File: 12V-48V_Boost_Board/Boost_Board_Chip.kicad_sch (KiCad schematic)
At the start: 23 parts, among them Q1 FDWS86068-F085

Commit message: Made all the changes, still working on the refining the track sizes
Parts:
- renumbered R8 to R10, R9 to R11, R3 to R5, R4 to R6, R5 to R7, R6 to R8, R7 to R9
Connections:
- net at C8.1, R6.2: now also R8.1; no longer R8.2
- net at U1.4 (GATE): now also Q1.4 (G); no longer Q1.3 (G)
- new net: Q1.8 (S), R8.2, R9.1
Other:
- moved on the sheet: Q1, R8
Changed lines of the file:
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@@
 	)
 	(junction
-		(at 175.26 60.96)
-		(diameter 0)
-		(color 0 0 0 0)
-	)
-	(junction
 		(at 172.72 90.17)
 		(diameter 0)
@@
 	)
 	(junction
+		(at 176.53 60.96)
+		(diameter 0)
+		(color 0 0 0 0)
+	)
+	(junction
 		(at 128.27 71.12)
 		(diameter 0)
@@
 	(wire
 		(pts
-			(xy 144.78 71.12) (xy 167.64 71.12)
+			(xy 144.78 71.12) (xy 168.91 71.12)
 		)
 		(stroke
@@
 	(wire
 		(pts
-			(xy 116.84 60.96) (xy 175.26 60.96)
+			(xy 116.84 60.96) (xy 176.53 60.96)
 		)
 		(stroke
@@
 	(wire
 		(pts
-			(xy 43.18 60.96) (xy 52.07 60.96)
+			(xy 176.53 60.96) (xy 196.85 60.96)
 		)
 		(stroke
@@
 	(wire
 		(pts
-			(xy 166.37 93.98) (xy 166.37 124.46)
+			(xy 43.18 60.96) (xy 52.07 60.96)
 		)
 		(stroke
@@
 	(wire
 		(pts
-			(xy 53.34 93.98) (xy 53.34 95.25)
+			(xy 166.37 93.98) (xy 166.37 124.46)
 		)
 		(stroke
@@
 	(wire
 		(pts
-			(xy 43.18 93.98) (xy 53.34 93.98)
+			(xy 53.34 93.98) (xy 53.34 95.25)
 		)
 		(stroke
@@
 	(wire
 		(pts
-			(xy 91.44 64.77) (xy 91.44 60.96)
+			(xy 43.18 93.98) (xy 53.34 93.98)
 		)
 		(stroke
@@
 	(wire
 		(pts
-			(xy 250.19 109.22) (xy 250.19 118.11)
+			(xy 91.44 64.77) (xy 91.44 60.96)
 		)
 		(stroke
@@
 	(wire
 		(pts
-			(xy 52.07 86.36) (xy 52.07 60.96)
+			(xy 250.19 109.22) (xy 250.19 118.11)
 		)
 		(stroke
@@
 	(wire
 		(pts
-			(xy 175.26 76.2) (xy 189.23 76.2)
+			(xy 52.07 86.36) (xy 52.07 60.96)
 		)
 		(stroke
@@
 	(wire
 		(pts
-			(xy 175.26 60.96) (xy 196.85 60.96)
+			(xy 176.53 76.2) (xy 189.23 76.2)
 		)
 		(stroke
@@
 	(wire
 		(pts
-			(xy 175.26 60.96) (xy 175.26 66.04)
+			(xy 176.53 60.96) (xy 176.53 66.04)
 		)
 		(stroke
@@
 		(dnp no)
 		(fields_autoplaced yes)
-		(property "Reference" "R7"
+		(property "Reference" "R9"
 			(at 191.77 101.5999 0)
 			(effects
@@
 			(project "12V-48V_Boost_Board"
 				(path "/3a220cd2-54b9-463d-ba95-4a8308a2a2d6/5e4f9813-0913-4f01-9ef9-037c6221a469"
-					(reference "R7")
+					(reference "R9")
 					(unit 1)
 				)
@@
 		(dnp no)
 		(fields_autoplaced yes)
-		(property "Reference" "R8"
+		(property "Reference" "R10"
 			(at 223.52 81.2799 0)
 			(effects
@@
 			(project "12V-48V_Boost_Board"
 				(path "/3a220cd2-54b9-463d-ba95-4a8308a2a2d6/5e4f9813-0913-4f01-9ef9-037c6221a469"
-					(reference "R8")
+					(reference "R10")
 					(unit 1)
 				)
@@
 	(symbol
 		(lib_id "Device:Q_NMOS_DSG")
-		(at 172.72 71.12 0)
+		(at 173.99 71.12 0)
 		(unit 1)
 		(exclude_from_sim no)
@@
 		(fields_autoplaced yes)
 		(property "Reference" "Q1"
-			(at 179.07 69.8499 0)
+			(at 180.34 69.8499 0)
 			(effects
 				(font
@@
 		)
 		(property "Value" "FDWS86068-F085"
-			(at 179.07 72.3899 0)
+			(at 180.34 72.3899 0)
 			(effects
 				(font
@@
 		)
 		(property "Footprint" "12/48 boost:Q1 Mosfet"
-			(at 177.8 68.58 0)
+			(at 179.07 68.58 0)
 			(effects
 				(font
@@
 		)
 		(property "Datasheet" "https://www.onsemi.com/download/data-sheet/pdf/fdws86068-f085-d.pdf"
-			(at 172.72 71.12 0)
+			(at 173.99 71.12 0)
 			(effects
 				(font
@@
 		)
 		(property "Description" "N-MOSFET transistor, drain/source/gate"
-			(at 172.72 71.12 0)
+			(at 173.99 71.12 0)
 			(effects
 				(font
@@
 		(pin "1"
 		)
-		(pin "2"
+		(pin "4"
 		)
-		(pin "3"
+		(pin "8"
 		)
 		(instances
@@
 		(dnp no)
 		(fields_autoplaced yes)
-		(property "Reference" "R9"
+		(property "Reference" "R11"
 			(at 223.52 129.5399 0)
 			(effects
@@
 			(project "12V-48V_Boost_Board"
 				(path "/3a220cd2-54b9-463d-ba95-4a8308a2a2d6/5e4f9813-0913-4f01-9ef9-037c6221a469"
-					(reference "R9")
+					(reference "R11")
 					(unit 1)
 				)
@@
 		(dnp no)
 		(fields_autoplaced yes)
-		(property "Reference" "R4"
+		(property "Reference" "R6"
 			(at 152.4 83.82 90)
 			(effects
@@
 			(project "12V-48V_Boost_Board"
 				(path "/3a220cd2-54b9-463d-ba95-4a8308a2a2d6/5e4f9813-0913-4f01-9ef9-037c6221a469"
-					(reference "R4")
+					(reference "R6")
 					(unit 1)
 				)
@@
 		(dnp no)
 		(fields_autoplaced yes)
-		(property "Reference" "R3"
+		(property "Reference" "R5"
 			(at 71.12 110.4899 0)
 			(effects
@@
 			(project "12V-48V_Boost_Board"
 				(path "/3a220cd2-54b9-463d-ba95-4a8308a2a2d6/5e4f9813-0913-4f01-9ef9-037c6221a469"
-					(reference "R3")
+					(reference "R5")
 					(unit 1)
 				)
@@
 		(dnp no)
 		(fields_autoplaced yes)
-		(property "Reference" "R5"
+		(property "Reference" "R7"
 			(at 154.94 130.8099 0)
 			(effects
@@
 			(project "12V-48V_Boost_Board"
 				(path "/3a220cd2-54b9-463d-ba95-4a8308a2a2d6/5e4f9813-0913-4f01-9ef9-037c6221a469"
-					(reference "R5")
+					(reference "R7")
 					(unit 1)
 				)
@@
 	(symbol
 		(lib_id "Device:R_US")
-		(at 180.34 90.17 270)
+		(at 180.34 90.17 90)
 		(unit 1)
 		(exclude_from_sim no)
@@
 		(dnp no)
 		(fields_autoplaced yes)
-		(property "Reference" "R6"
+		(property "Reference" "R8"
 			(at 180.34 83.82 90)
 			(effects
@@
 		)
 		(property "Footprint" "Resistor_SMD:R_0805_2012Metric_Pad1.20x1.40mm_HandSolder"
-			(at 180.086 91.186 90)
+			(at 180.594 89.154 90)
 			(effects
 				(font
@@
 			(project "12V-48V_Boost_Board"
 				(path "/3a220cd2-54b9-463d-ba95-4a8308a2a2d6/5e4f9813-0913-4f01-9ef9-037c6221a469"
-					(reference "R6")
+					(reference "R8")
 					(unit 1)
 				)

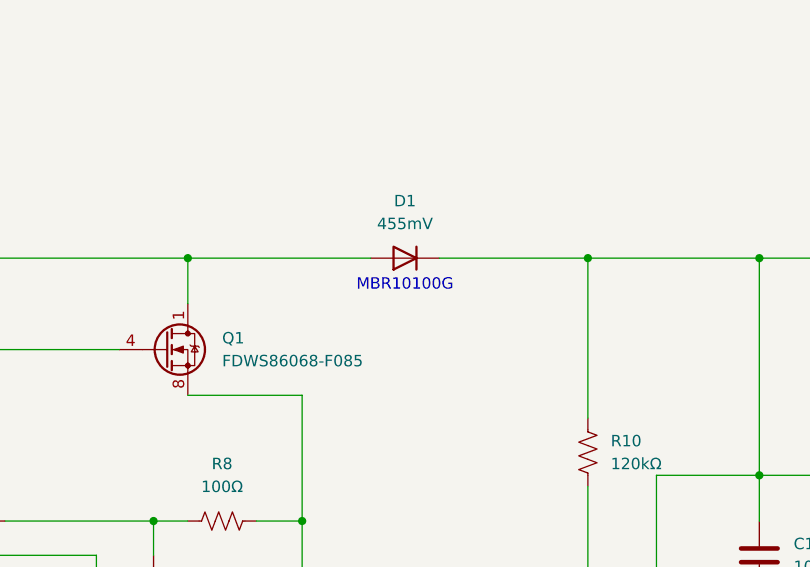
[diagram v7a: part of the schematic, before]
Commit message: Made some changes to track sizes
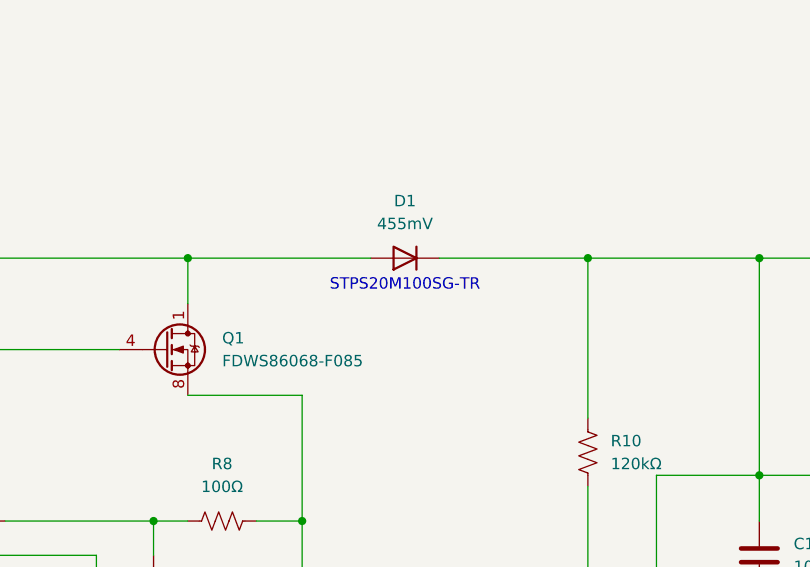
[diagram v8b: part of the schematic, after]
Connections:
- net 48V_OUTPUT: now also D1.3 (K); no longer D1.1 (K)
- net at L1.2, Q1.1 (D): now also D1.1 (A); no longer D1.2 (A)
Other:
- note added: "STPS20M100SG-TR"
- note removed: "MBR10100G"
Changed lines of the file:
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@@
 		)
 	)
-	(text "MBR10100G"
+	(text "STPS20M100SG-TR"
 		(exclude_from_sim no)
 		(at 200.66 64.008 0)
@@
 		)
 		(property "Footprint" "12/48 boost:D2PAK_STM-M"
-			(at 200.66 60.96 0)
+			(at 200.406 58.166 0)
 			(effects
 				(font
@@
 			)
 		)
-		(property "Sim.Pins" "1=K 2=A"
-			(at 200.66 60.96 0)
-			(effects
-				(font
-					(size 1.27 1.27)
-				)
-				(hide yes)
-			)
-		)
-		(pin "1"
-		)
-		(pin "2"
-		)
-		(instances
+		(property "Sim.Pins" "3=K 1=A"
+			(at 201.168 58.674 0)
+			(effects
+				(font
+					(size 1.27 1.27)
+				)
+				(hide yes)
+			)
+		)
+		(pin "1"
+		)
+		(pin "3"
+		)
+		(instances
